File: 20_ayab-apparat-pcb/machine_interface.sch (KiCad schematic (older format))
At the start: 12 parts

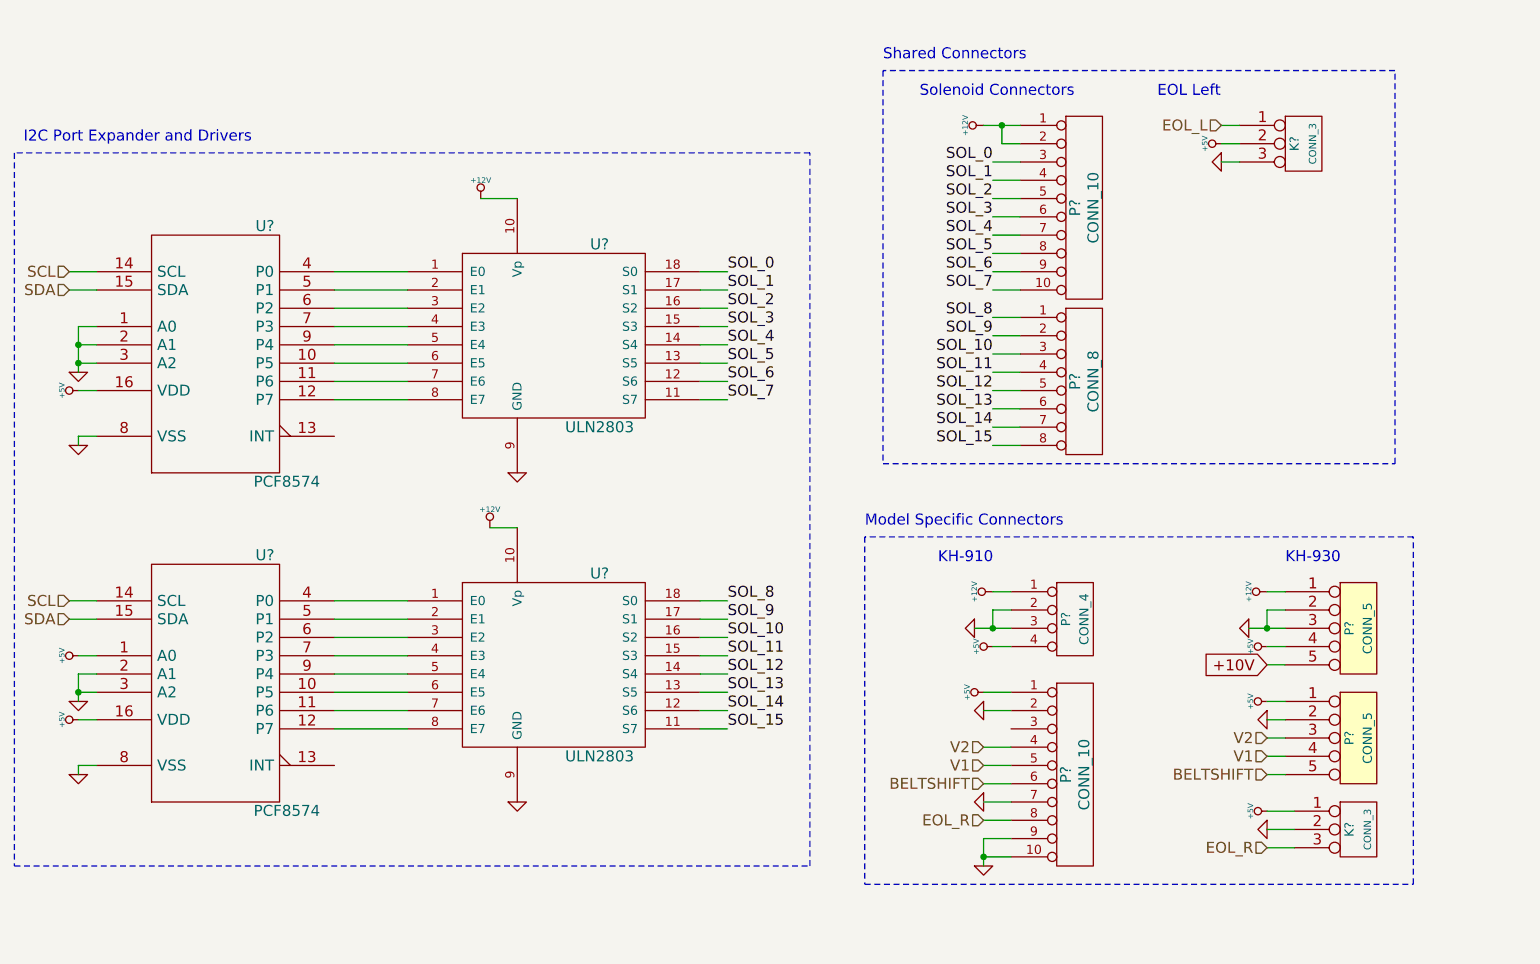
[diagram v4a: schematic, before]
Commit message: added partnames and values, generated first version of netlist, ready to assign footprints
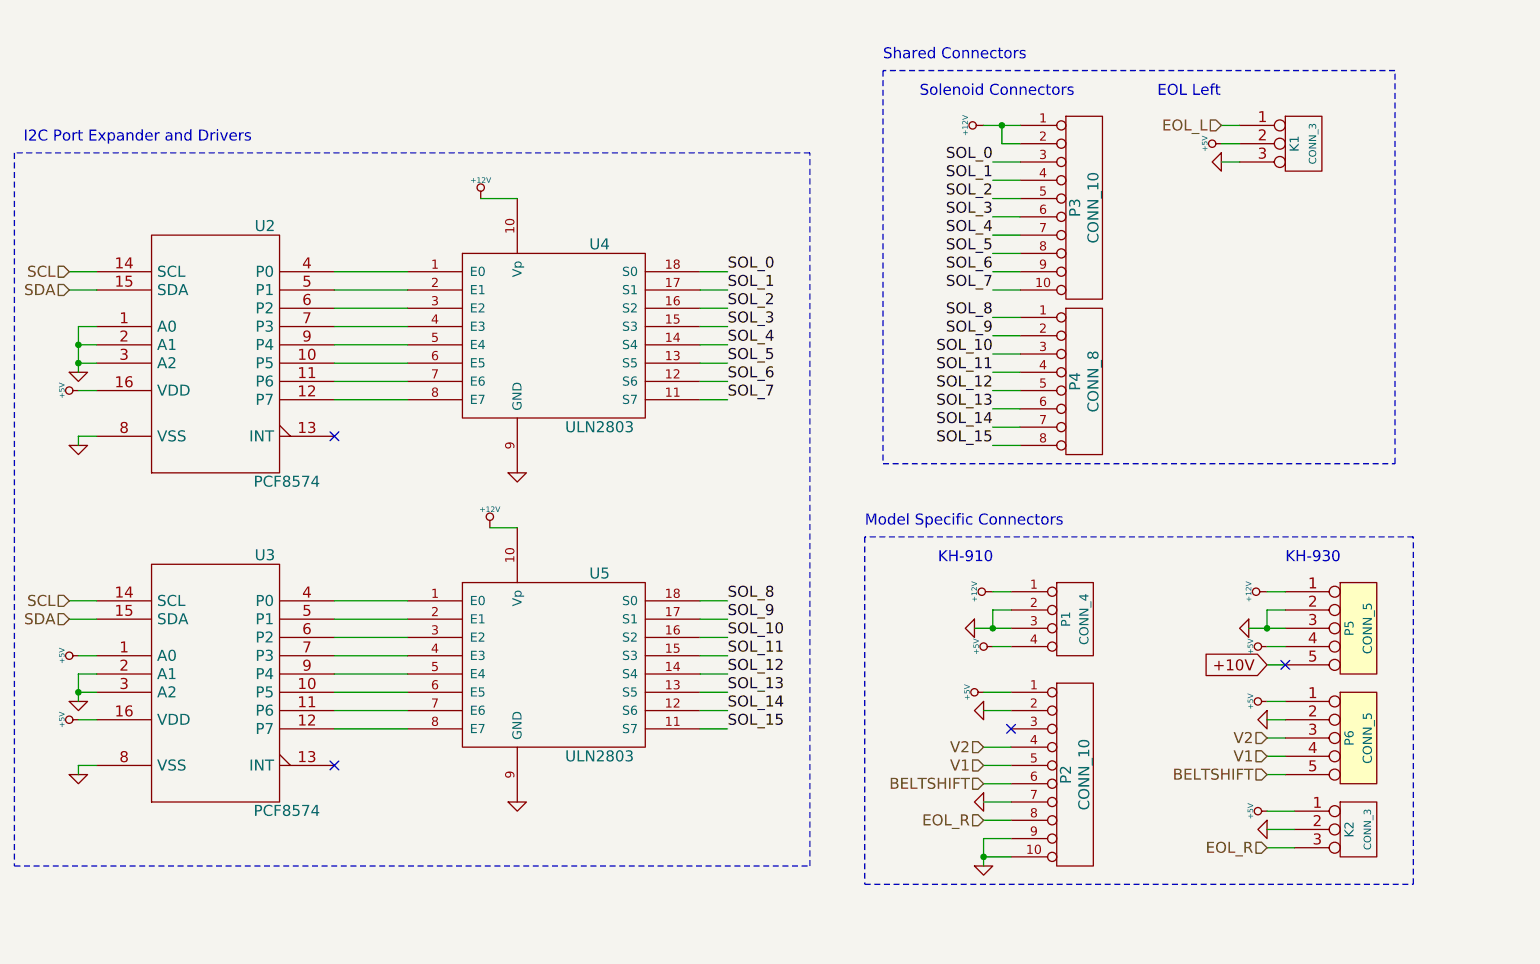
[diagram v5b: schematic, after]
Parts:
- gave numbers to parts that had none: 12
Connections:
- no-connect marks 0 -> 4
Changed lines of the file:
@@
 $EndDescr
 $Comp
-L CONN_10 P?
+L CONN_10 P3
 U 1 1 52E14DAF
 P 6900 1900
-F 0 "P?" V 6850 1900 60  0000 C CNN
+F 0 "P3" V 6850 1900 60  0000 C CNN
 F 1 "CONN_10" V 6950 1900 60  0000 C CNN
 F 2 "" H 6900 1900 60  0000 C CNN
@@
 $EndComp
 $Comp
-L CONN_4 P?
+L CONN_4 P1
 U 1 1 52E14DC5
 P 6850 4150
-F 0 "P?" V 6800 4150 50  0000 C CNN
+F 0 "P1" V 6800 4150 50  0000 C CNN
 F 1 "CONN_4" V 6900 4150 50  0000 C CNN
 F 2 "" H 6850 4150 60  0000 C CNN
@@
 $EndComp
 $Comp
-L CONN_3 K?
+L CONN_3 K1
 U 1 1 52E14DD9
 P 8100 1550
-F 0 "K?" V 8050 1550 50  0000 C CNN
+F 0 "K1" V 8050 1550 50  0000 C CNN
 F 1 "CONN_3" V 8150 1550 40  0000 C CNN
 F 2 "" H 8100 1550 60  0000 C CNN
@@
 $EndComp
 $Comp
-L CONN_8 P?
+L CONN_8 P4
 U 1 1 52E14DED
 P 6900 2850
-F 0 "P?" V 6850 2850 60  0000 C CNN
+F 0 "P4" V 6850 2850 60  0000 C CNN
 F 1 "CONN_8" V 6950 2850 60  0000 C CNN
 F 2 "" H 6900 2850 60  0000 C CNN
@@
 $EndComp
 $Comp
-L CONN_10 P?
+L CONN_10 P2
 U 1 1 52E14E01
 P 6850 5000
-F 0 "P?" V 6800 5000 60  0000 C CNN
+F 0 "P2" V 6800 5000 60  0000 C CNN
 F 1 "CONN_10" V 6900 5000 60  0000 C CNN
 F 2 "" H 6850 5000 60  0000 C CNN
@@
 EOL_L
 $Comp
-L +5V #PWR?
+L +5V #PWR06
 U 1 1 52E1540D
 P 7650 1550
-F 0 "#PWR?" H 7650 1640 20  0001 C CNN
+F 0 "#PWR06" H 7650 1640 20  0001 C CNN
 F 1 "+5V" H 7650 1640 30  0000 C CNN
 F 2 "" H 7650 1550 60  0000 C CNN
@@
 $EndComp
 $Comp
-L GND #PWR?
+L GND #PWR07
 U 1 1 52E15421
 P 7650 1650
-F 0 "#PWR?" H 7650 1650 30  0001 C CNN
+F 0 "#PWR07" H 7650 1650 30  0001 C CNN
 F 1 "GND" H 7650 1580 30  0001 C CNN
 F 2 "" H 7650 1650 60  0000 C CNN
@@
 $EndComp
 $Comp
-L GND #PWR?
+L GND #PWR08
 U 1 1 52E15472
 P 6300 4200
-F 0 "#PWR?" H 6300 4200 30  0001 C CNN
+F 0 "#PWR08" H 6300 4200 30  0001 C CNN
 F 1 "GND" H 6300 4130 30  0001 C CNN
 F 2 "" H 6300 4200 60  0000 C CNN
@@
 $EndComp
 $Comp
-L +5V #PWR?
+L +5V #PWR09
 U 1 1 52E15500
 P 6400 4300
-F 0 "#PWR?" H 6400 4390 20  0001 C CNN
+F 0 "#PWR09" H 6400 4390 20  0001 C CNN
 F 1 "+5V" H 6400 4390 30  0000 C CNN
 F 2 "" H 6400 4300 60  0000 C CNN
@@
 KH-910
 $Comp
-L PCF8574 U?
+L PCF8574 U2
 U 1 1 52E15707
 P 2150 2700
-F 0 "U?" H 2420 3400 60  0000 C CNN
+F 0 "U2" H 2420 3400 60  0000 C CNN
 F 1 "PCF8574" H 2540 2002 60  0000 C CNN
 F 2 "" H 2150 2700 60  0000 C CNN
@@
 $EndComp
 $Comp
-L PCF8574 U?
+L PCF8574 U3
 U 1 1 52E1571B
 P 2150 4500
-F 0 "U?" H 2420 5200 60  0000 C CNN
+F 0 "U3" H 2420 5200 60  0000 C CNN
 F 1 "PCF8574" H 2540 3802 60  0000 C CNN
 F 2 "" H 2150 4500 60  0000 C CNN
@@
 $EndComp
 $Comp
-L ULN2803 U?
+L ULN2803 U4
 U 1 1 52E157BC
 P 4000 2600
-F 0 "U?" H 4250 3100 60  0000 C CNN
+F 0 "U4" H 4250 3100 60  0000 C CNN
 F 1 "ULN2803" H 4250 2100 60  0000 C CNN
 F 2 "" H 4000 2600 60  0000 C CNN
@@
 $EndComp
 $Comp
-L ULN2803 U?
+L ULN2803 U5
 U 1 1 52E157D0
 P 4000 4400
-F 0 "U?" H 4250 4900 60  0000 C CNN
+F 0 "U5" H 4250 4900 60  0000 C CNN
 F 1 "ULN2803" H 4250 3900 60  0000 C CNN
 F 2 "" H 4000 4400 60  0000 C CNN
@@
 $EndComp
 $Comp
-L GND #PWR?
+L GND #PWR010
 U 1 1 52E1590C
 P 3800 3350
-F 0 "#PWR?" H 3800 3350 30  0001 C CNN
+F 0 "#PWR010" H 3800 3350 30  0001 C CNN
 F 1 "GND" H 3800 3280 30  0001 C CNN
 F 2 "" H 3800 3350 60  0000 C CNN
@@
 $EndComp
 $Comp
-L GND #PWR?
+L GND #PWR011
 U 1 1 52E15921
 P 3800 5150
-F 0 "#PWR?" H 3800 5150 30  0001 C CNN
+F 0 "#PWR011" H 3800 5150 30  0001 C CNN
 F 1 "GND" H 3800 5080 30  0001 C CNN
 F 2 "" H 3800 5150 60  0000 C CNN
@@
 $EndComp
 $Comp
-L GND #PWR?
+L GND #PWR012
 U 1 1 52E6C9F8
 P 1400 3200
-F 0 "#PWR?" H 1400 3200 30  0001 C CNN
+F 0 "#PWR012" H 1400 3200 30  0001 C CNN
 F 1 "GND" H 1400 3130 30  0001 C CNN
 F 2 "" H 1400 3200 60  0000 C CNN
@@
 $EndComp
 $Comp
-L +5V #PWR?
+L +5V #PWR013
 U 1 1 52E6CA3F
 P 1400 2900
-F 0 "#PWR?" H 1400 2990 20  0001 C CNN
+F 0 "#PWR013" H 1400 2990 20  0001 C CNN
 F 1 "+5V" H 1400 2990 30  0000 C CNN
 F 2 "" H 1400 2900 60  0000 C CNN
@@
 $EndComp
 $Comp
-L GND #PWR?
+L GND #PWR014
 U 1 1 52E6CA86
 P 1400 2800
-F 0 "#PWR?" H 1400 2800 30  0001 C CNN
+F 0 "#PWR014" H 1400 2800 30  0001 C CNN
 F 1 "GND" H 1400 2730 30  0001 C CNN
 F 2 "" H 1400 2800 60  0000 C CNN
@@
 $EndComp
 $Comp
-L GND #PWR?
+L GND #PWR015
 U 1 1 52E6CB3E
 P 1400 5000
-F 0 "#PWR?" H 1400 5000 30  0001 C CNN
+F 0 "#PWR015" H 1400 5000 30  0001 C CNN
 F 1 "GND" H 1400 4930 30  0001 C CNN
 F 2 "" H 1400 5000 60  0000 C CNN
@@
 $EndComp
 $Comp
-L GND #PWR?
+L GND #PWR016
 U 1 1 52E6CB52
 P 1400 4600
-F 0 "#PWR?" H 1400 4600 30  0001 C CNN
+F 0 "#PWR016" H 1400 4600 30  0001 C CNN
 F 1 "GND" H 1400 4530 30  0001 C CNN
 F 2 "" H 1400 4600 60  0000 C CNN
@@
 $EndComp
 $Comp
-L +5V #PWR?
+L +5V #PWR017
 U 1 1 52E6CB66
 P 1400 4700
-F 0 "#PWR?" H 1400 4790 20  0001 C CNN
+F 0 "#PWR017" H 1400 4790 20  0001 C CNN
 F 1 "+5V" H 1400 4790 30  0000 C CNN
 F 2 "" H 1400 4700 60  0000 C CNN
@@
 $EndComp
 $Comp
-L +5V #PWR?
+L +5V #PWR018
 U 1 1 52E6CB7A
 P 1400 4350
-F 0 "#PWR?" H 1400 4440 20  0001 C CNN
+F 0 "#PWR018" H 1400 4440 20  0001 C CNN
 F 1 "+5V" H 1400 4440 30  0000 C CNN
 F 2 "" H 1400 4350 60  0000 C CNN
@@
 SCL
 $Comp
-L +5V #PWR?
+L +5V #PWR019
 U 1 1 52E6CE5D
 P 6350 4550
-F 0 "#PWR?" H 6350 4640 20  0001 C CNN
+F 0 "#PWR019" H 6350 4640 20  0001 C CNN
 F 1 "+5V" H 6350 4640 30  0000 C CNN
 F 2 "" H 6350 4550 60  0000 C CNN
@@
 $EndComp
 $Comp
-L GND #PWR?
+L GND #PWR020
 U 1 1 52E6CE71
 P 6350 4650
-F 0 "#PWR?" H 6350 4650 30  0001 C CNN
+F 0 "#PWR020" H 6350 4650 30  0001 C CNN
 F 1 "GND" H 6350 4580 30  0001 C CNN
 F 2 "" H 6350 4650 60  0000 C CNN
@@
 $EndComp
 $Comp
-L GND #PWR?
+L GND #PWR021
 U 1 1 52E6CE94
 P 6350 5500
-F 0 "#PWR?" H 6350 5500 30  0001 C CNN
+F 0 "#PWR021" H 6350 5500 30  0001 C CNN
 F 1 "GND" H 6350 5430 30  0001 C CNN
 F 2 "" H 6350 5500 60  0000 C CNN
@@
 $EndComp
 $Comp
-L GND #PWR?
+L GND #PWR022
 U 1 1 52E6CF37
 P 6350 5150
-F 0 "#PWR?" H 6350 5150 30  0001 C CNN
+F 0 "#PWR022" H 6350 5150 30  0001 C CNN
 F 1 "GND" H 6350 5080 30  0001 C CNN
 F 2 "" H 6350 5150 60  0000 C CNN
@@
 Solenoid Connectors
 $Comp
-L CONN_5 P?
+L CONN_5 P6
 U 1 1 52E7E6BB
 P 8400 4800
-F 0 "P?" V 8350 4800 50  0000 C CNN
+F 0 "P6" V 8350 4800 50  0000 C CNN
 F 1 "CONN_5" V 8450 4800 50  0000 C CNN
 F 2 "" H 8400 4800 60  0000 C CNN
@@
 $EndComp
 $Comp
-L CONN_3 K?
+L CONN_3 K2
 U 1 1 52E7E6D3
 P 8400 5300
-F 0 "K?" V 8350 5300 50  0000 C CNN
+F 0 "K2" V 8350 5300 50  0000 C CNN
 F 1 "CONN_3" V 8450 5300 40  0000 C CNN
 F 2 "" H 8400 5300 60  0000 C CNN
@@
 $EndComp
 $Comp
-L CONN_5 P?
+L CONN_5 P5
 U 1 1 52E7E6E7
 P 8400 4200
-F 0 "P?" V 8350 4200 50  0000 C CNN
+F 0 "P5" V 8350 4200 50  0000 C CNN
 F 1 "CONN_5" V 8450 4200 50  0000 C CNN
 F 2 "" H 8400 4200 60  0000 C CNN
@@
 Model Specific Connectors
 $Comp
-L GND #PWR?
+L GND #PWR023
 U 1 1 52E7E76D
 P 7800 4200
-F 0 "#PWR?" H 7800 4200 30  0001 C CNN
+F 0 "#PWR023" H 7800 4200 30  0001 C CNN
 F 1 "GND" H 7800 4130 30  0001 C CNN
 F 2 "" H 7800 4200 60  0000 C CNN
@@
 $EndComp
 $Comp
-L +5V #PWR?
+L +5V #PWR024
 U 1 1 52E7E781
 P 7900 4300
-F 0 "#PWR?" H 7900 4390 20  0001 C CNN
+F 0 "#PWR024" H 7900 4390 20  0001 C CNN
 F 1 "+5V" H 7900 4390 30  0000 C CNN
 F 2 "" H 7900 4300 60  0000 C CNN
@@
 	7900 4400 8000 4400
 $Comp
-L +5V #PWR?
+L +5V #PWR025
 U 1 1 52E7EA73
 P 7900 5200
-F 0 "#PWR?" H 7900 5290 20  0001 C CNN
+F 0 "#PWR025" H 7900 5290 20  0001 C CNN
 F 1 "+5V" H 7900 5290 30  0000 C CNN
 F 2 "" H 7900 5200 60  0000 C CNN
@@
 $EndComp
 $Comp
-L GND #PWR?
+L GND #PWR026
 U 1 1 52E7EA87
 P 7900 5300
-F 0 "#PWR?" H 7900 5300 30  0001 C CNN
+F 0 "#PWR026" H 7900 5300 30  0001 C CNN
 F 1 "GND" H 7900 5230 30  0001 C CNN
 F 2 "" H 7900 5300 60  0000 C CNN
@@
 	7900 5200 8050 5200
 $Comp
-L +5V #PWR?
+L +5V #PWR027
 U 1 1 52E7ECB1
 P 7900 4600
-F 0 "#PWR?" H 7900 4690 20  0001 C CNN
+F 0 "#PWR027" H 7900 4690 20  0001 C CNN
 F 1 "+5V" H 7900 4690 30  0000 C CNN
 F 2 "" H 7900 4600 60  0000 C CNN
@@
 $EndComp
 $Comp
-L GND #PWR?
+L GND #PWR028
 U 1 1 52E7ECD1
 P 7900 4700
-F 0 "#PWR?" H 7900 4700 30  0001 C CNN
+F 0 "#PWR028" H 7900 4700 30  0001 C CNN
 F 1 "GND" H 7900 4630 30  0001 C CNN
 F 2 "" H 7900 4700 60  0000 C CNN
@@
 	8600 1150 5800 1150
 $Comp
-L +12V #PWR?
+L +12V #PWR029
 U 1 1 52EA8D08
 P 6400 4000
-F 0 "#PWR?" H 6400 3950 20  0001 C CNN
+F 0 "#PWR029" H 6400 3950 20  0001 C CNN
 F 1 "+12V" H 6400 4100 30  0000 C CNN
 F 2 "" H 6400 4000 60  0000 C CNN
@@
 $EndComp
 $Comp
-L +12V #PWR?
+L +12V #PWR030
 U 1 1 52EA8D1C
 P 7900 4000
-F 0 "#PWR?" H 7900 3950 20  0001 C CNN
+F 0 "#PWR030" H 7900 3950 20  0001 C CNN
 F 1 "+12V" H 7900 4100 30  0000 C CNN
 F 2 "" H 7900 4000 60  0000 C CNN
@@
 $EndComp
 $Comp
-L +12V #PWR?
+L +12V #PWR031
 U 1 1 52EA8D30
 P 6350 1450
-F 0 "#PWR?" H 6350 1400 20  0001 C CNN
+F 0 "#PWR031" H 6350 1400 20  0001 C CNN
 F 1 "+12V" H 6350 1550 30  0000 C CNN
 F 2 "" H 6350 1450 60  0000 C CNN
@@
 $EndComp
 $Comp
-L +12V #PWR?
+L +12V #PWR032
 U 1 1 52EA8D44
 P 3600 1850
-F 0 "#PWR?" H 3600 1800 20  0001 C CNN
+F 0 "#PWR032" H 3600 1800 20  0001 C CNN
 F 1 "+12V" H 3600 1950 30  0000 C CNN
 F 2 "" H 3600 1850 60  0000 C CNN
@@
 $EndComp
 $Comp
-L +12V #PWR?
+L +12V #PWR033
 U 1 1 52EA8D58
 P 3650 3650
-F 0 "#PWR?" H 3650 3600 20  0001 C CNN
+F 0 "#PWR033" H 3650 3600 20  0001 C CNN
 F 1 "+12V" H 3650 3750 30  0000 C CNN
 F 2 "" H 3650 3650 60  0000 C CNN
@@
 	1    0    0    -1
 $EndComp
+NoConn ~ 8000 4400
+NoConn ~ 2800 3150
+NoConn ~ 2800 4950
+NoConn ~ 6500 4750
 $EndSCHEMATC
